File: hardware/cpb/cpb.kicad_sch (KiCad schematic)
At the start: 122 parts, among them J1 Conn_02x20_Odd_Even, J10 SW1, J11 SW2, J12 SW3, J13 PISW1, J14 μSW1, J15 μSW2, J16 μSW3, J17 μSW4, J2 I2CExt, J3 DAC1BUF, J4 DAC2BUF, J6 Conn_02x20_Odd_Even, J7 ADC6/7, J8 ADC2/3, J9 4FBRG, J99 RBFJUMP, Q1 PMBT2222A, Q2 IRF9393, Q3 MBT2222ADW1T1, Q4 PMBT2222A, U1 TS912, U2 ADR420ARMZ, U3 KF33BDT, U4 STM32L072R_B-Z_Tx, U5 AP63205WU, U6 SC16IS750xBS, Y1 14.7456MHz

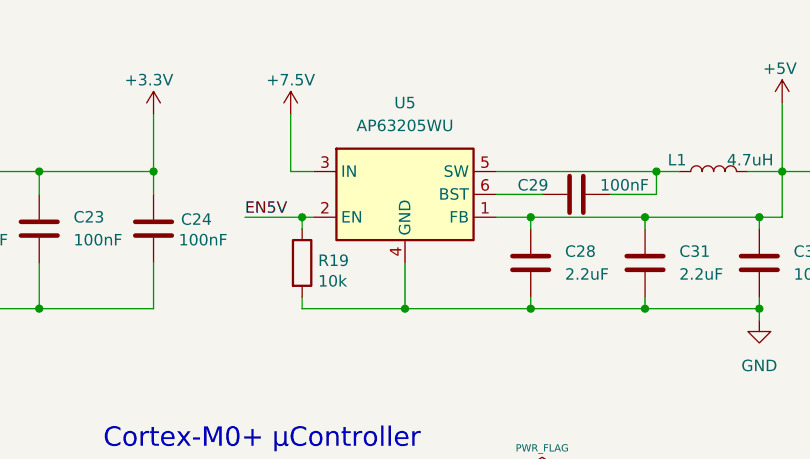
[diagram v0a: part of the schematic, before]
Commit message: cpb: many, many fixes
- Move components to bottom to match design intent
- Adjust AP62305 to hopefully have correct pinout
- Replace manual RBF jumper with solder jumper: just not enough room
- High level adjustment to placement to ease layout.
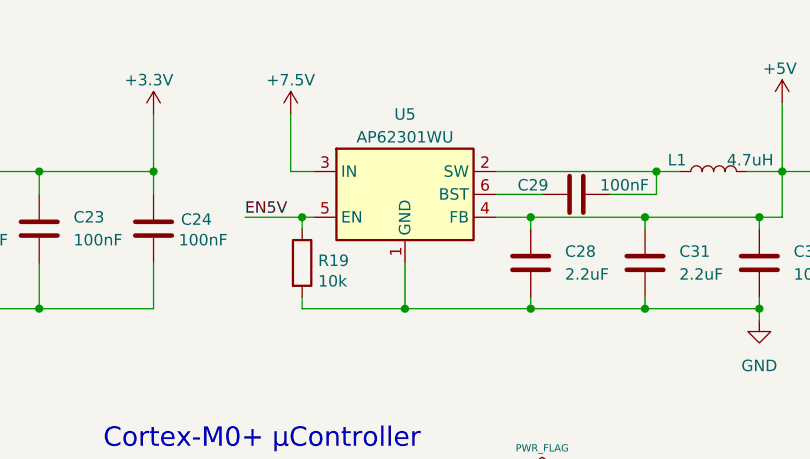
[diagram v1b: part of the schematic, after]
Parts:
- removed U5: AP63205WU, Package_TO_SOT_SMD:TSOT-23-6, symbol Regulator_Switching:AP63205WU
- added U5: AP62301WU, Package_TO_SOT_SMD:TSOT-23-6, symbol Regulator_Switching:AP62301WU
- J6: footprint Connector_PinHeader_2.54mm:PinHeader_2x20_P2.54mm_Vertical -> SSE_Footprints:RPI02W
- J99: footprint Connector_PinHeader_2.54mm:PinHeader_1x02_P2.54mm_Horizontal -> Jumper:SolderJumper-2_P1.3mm_Open_TrianglePad1.0x1.5mm
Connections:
- net +5V: now also U5.4 (FB)
- net +7.5V: now also U5.3 (IN)
- net EN5V: now also U5.5 (EN)
- net GND: now also U5.1 (GND)
- net at C29.2, L1.1: now also U5.2 (SW)
- net at C29.1: now also U5.6 (BST)
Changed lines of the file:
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@@
 	)
 	(symbol
+		(lib_id "Regulator_Switching:AP62301WU")
+		(at 205.74 31.75 0)
+		(unit 1)
+		(exclude_from_sim no)
+		(in_bom yes)
+		(on_board yes)
+		(dnp no)
+		(fields_autoplaced yes)
+		(property "Reference" "U5"
+			(at 205.74 22.86 0)
+			(effects
+				(font
+					(size 1.27 1.27)
+				)
+			)
+		)
+		(property "Value" "AP62301WU"
+			(at 205.74 25.4 0)
+			(effects
+				(font
+					(size 1.27 1.27)
+				)
+			)
+		)
+		(property "Footprint" "Package_TO_SOT_SMD:TSOT-23-6"
+			(at 205.74 54.61 0)
+			(effects
+				(font
+					(size 1.27 1.27)
+				)
+				(hide yes)
+			)
+		)
+		(property "Datasheet" "https://www.diodes.com/assets/Datasheets/AP62300_AP62301_AP62300T.pdf"
+			(at 205.74 31.75 0)
+			(effects
+				(font
+					(size 1.27 1.27)
+				)
+				(hide yes)
+			)
+		)
+		(property "Description" "3A, 750kHz Buck DC/DC Converter, 4.2V-18V input voltage, 0.8V-7V adjustable output voltage, TSOT-23-6"
+			(at 205.74 31.75 0)
+			(effects
+				(font
+					(size 1.27 1.27)
+				)
+				(hide yes)
+			)
+		)
+		(pin "6"
+		)
+		(pin "3"
+		)
+		(pin "5"
+		)
+		(pin "4"
+		)
+		(pin "1"
+		)
+		(pin "2"
+		)
+		(instances
+			(project "cpb"
+				(path "/9a10a1ee-db5a-47ad-90f3-81b92d74d449"
+					(reference "U5")
+					(unit 1)
+				)
+			)
+		)
+	)
+	(symbol
 		(lib_id "power:GND")
 		(at 193.04 224.79 0)
@@
 	)
 	(symbol
-		(lib_id "Regulator_Switching:AP63205WU")
-		(at 205.74 31.75 0)
-		(unit 1)
-		(exclude_from_sim no)
-		(in_bom yes)
-		(on_board yes)
-		(dnp no)
-		(fields_autoplaced yes)
-		(property "Reference" "U5"
-			(at 205.74 21.59 0)
-			(effects
-				(font
-					(size 1.27 1.27)
-				)
-			)
-		)
-		(property "Value" "AP63205WU"
-			(at 205.74 24.13 0)
-			(effects
-				(font
-					(size 1.27 1.27)
-				)
-			)
-		)
-		(property "Footprint" "Package_TO_SOT_SMD:TSOT-23-6"
-			(at 205.74 54.61 0)
-			(effects
-				(font
-					(size 1.27 1.27)
-				)
-				(hide yes)
-			)
-		)
-		(property "Datasheet" "https://www.diodes.com/assets/Datasheets/AP63200-AP63201-AP63203-AP63205.pdf"
-			(at 205.74 31.75 0)
-			(effects
-				(font
-					(size 1.27 1.27)
-				)
-				(hide yes)
-			)
-		)
-		(property "Description" "2A, 1.1MHz Buck DC/DC Converter, fixed 5.0V output voltage, TSOT-23-6"
-			(at 205.74 31.75 0)
-			(effects
-				(font
-					(size 1.27 1.27)
-				)
-				(hide yes)
-			)
-		)
-		(property "LCSC" "C2071056"
-			(at 205.74 31.75 0)
-			(effects
-				(font
-					(size 1.27 1.27)
-				)
-				(hide yes)
-			)
-		)
-		(pin "1"
-		)
-		(pin "2"
-		)
-		(pin "6"
-		)
-		(pin "5"
-		)
-		(pin "3"
-		)
-		(pin "4"
-		)
-		(instances
-			(project "cpb"
-				(path "/9a10a1ee-db5a-47ad-90f3-81b92d74d449"
-					(reference "U5")
-					(unit 1)
-				)
-			)
-		)
-	)
-	(symbol
 		(lib_id "power:GND")
 		(at 403.86 138.43 0)
@@
 			)
 		)
-		(property "Footprint" "Connector_PinHeader_2.54mm:PinHeader_1x02_P2.54mm_Horizontal"
+		(property "Footprint" "Jumper:SolderJumper-2_P1.3mm_Open_TrianglePad1.0x1.5mm"
 			(at 134.62 125.73 0)
 			(effects
@@
 			)
 		)
-		(property "Footprint" "Connector_PinHeader_2.54mm:PinHeader_2x20_P2.54mm_Vertical"
+		(property "Footprint" "SSE_Footprints:RPI02W"
 			(at 269.24 228.6 0)
 			(effects

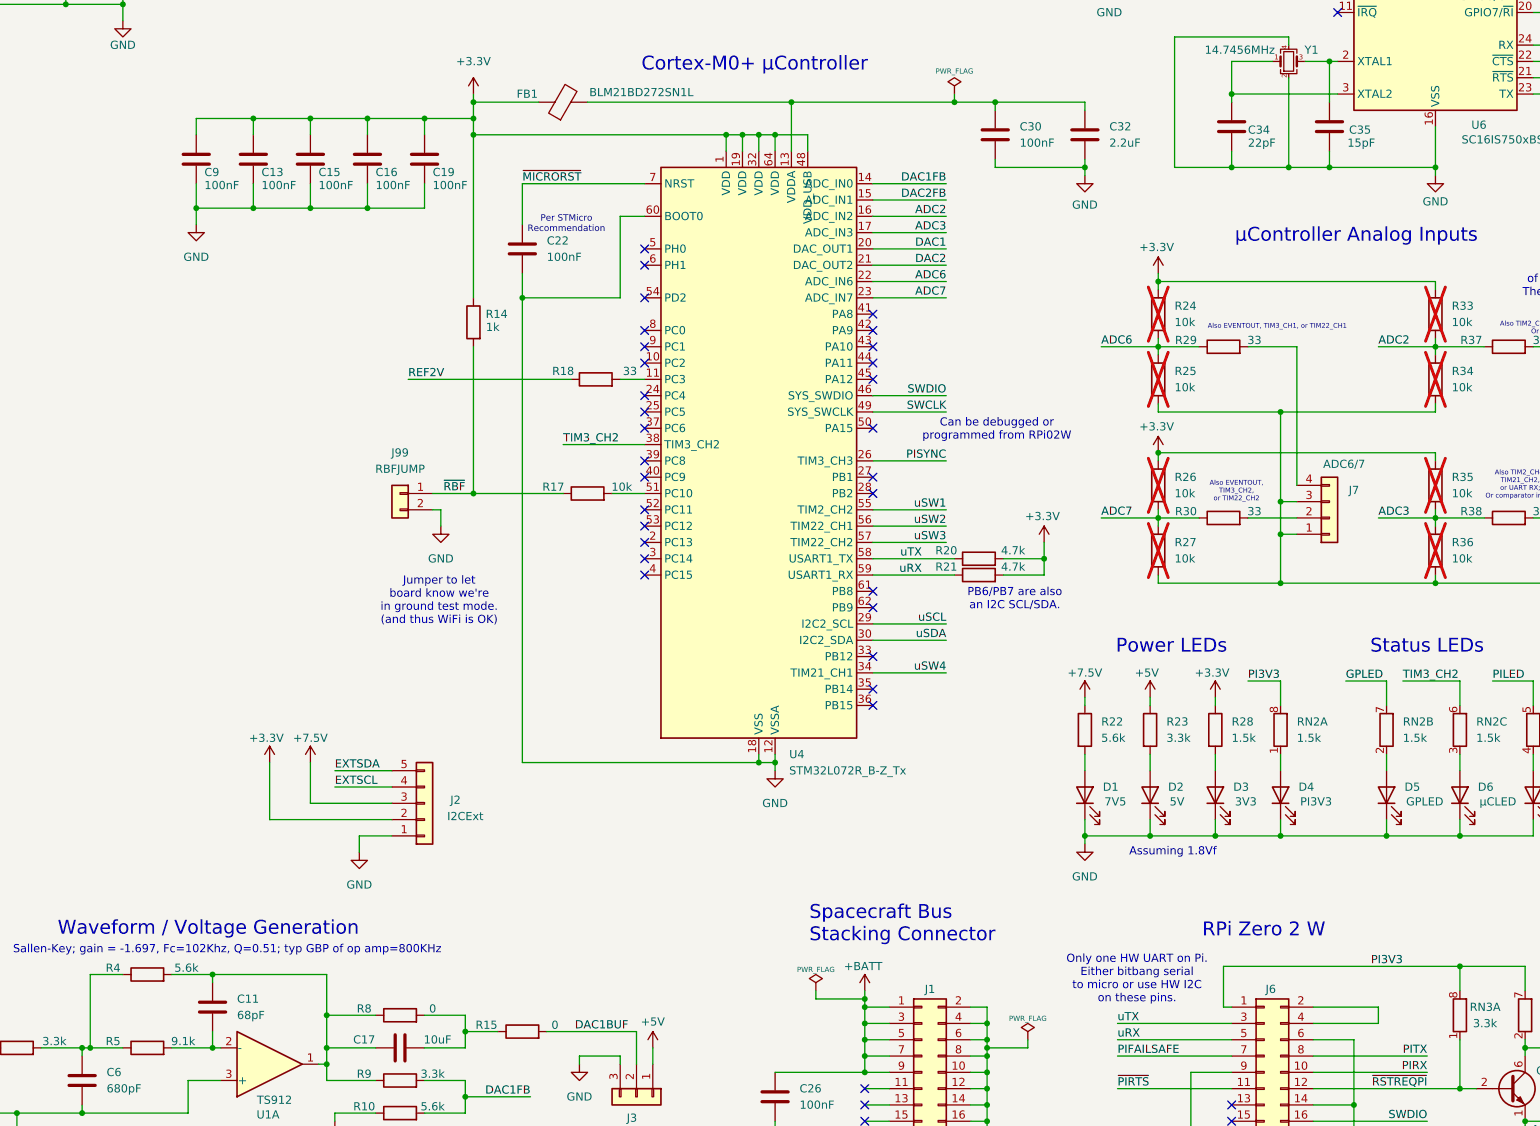
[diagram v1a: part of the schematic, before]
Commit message: cpb: complete placement
- add a capacitor to ensure we can bypass all 3V3 components well
- align components
- add copper pour regions
- a lot of effort on text, and legends for connectors

Plus probably much more...
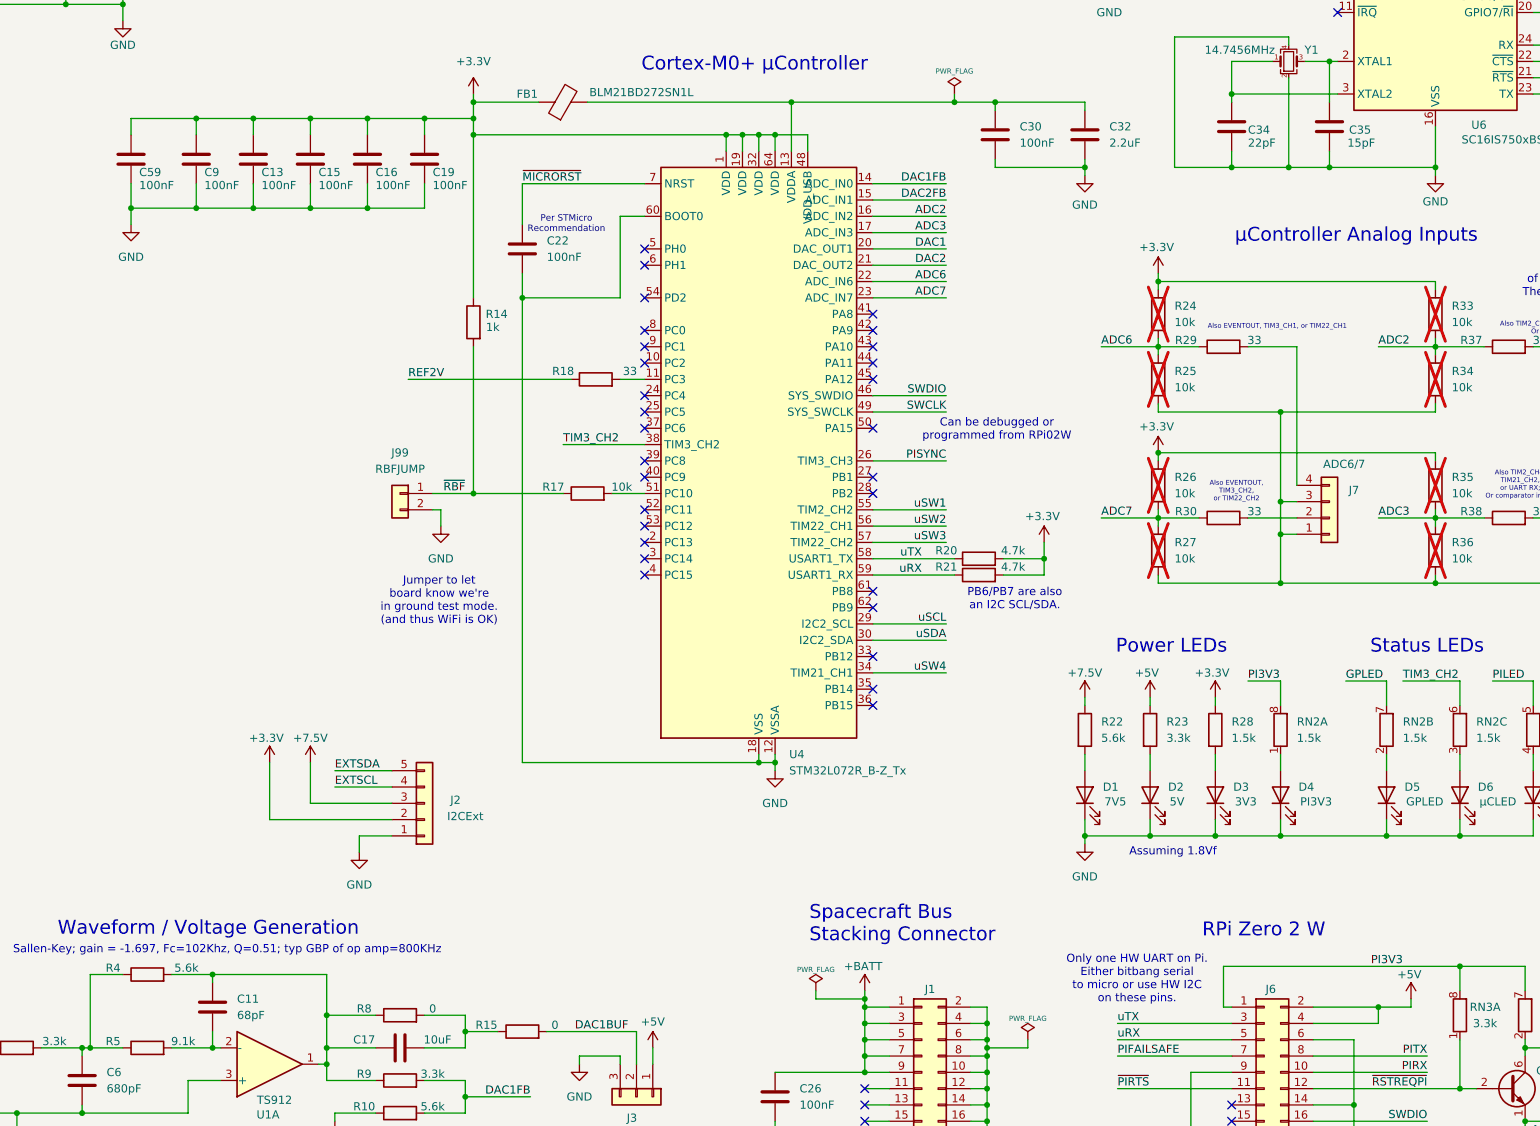
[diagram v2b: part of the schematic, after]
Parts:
- added C59: 100nF, Capacitor_SMD:C_0603_1608Metric, symbol Device:C
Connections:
- net +3.3V: now also C59.1
- net +5V: now also J6.2 (Pin_2), J6.4 (Pin_4)
- net GND: now also C59.2
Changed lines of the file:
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@@
 	)
 	(junction
+		(at 102.87 67.31)
+		(diameter 0)
+		(color 0 0 0 0)
+	)
+	(junction
 		(at 262.89 27.94)
 		(diameter 0)
@@
 	)
 	(junction
+		(at 92.71 81.28)
+		(diameter 0)
+		(color 0 0 0 0)
+	)
+	(junction
 		(at 299.72 218.44)
 		(diameter 0)
@@
 	)
 	(junction
+		(at 287.02 205.74)
+		(diameter 0)
+		(color 0 0 0 0)
+	)
+	(junction
 		(at 193.04 69.85)
 		(diameter 0)
@@
 	(wire
 		(pts
-			(xy 102.87 81.28) (xy 102.87 83.82)
+			(xy 92.71 81.28) (xy 92.71 83.82)
 		)
 		(stroke
@@
 	(wire
 		(pts
+			(xy 92.71 77.47) (xy 92.71 81.28)
+		)
+		(stroke
+			(width 0)
+			(type default)
+		)
+	)
+	(wire
+		(pts
 			(xy 146.05 125.73) (xy 160.02 125.73)
 		)
@@
 	(wire
 		(pts
+			(xy 92.71 69.85) (xy 92.71 67.31)
+		)
+		(stroke
+			(width 0)
+			(type default)
+		)
+	)
+	(wire
+		(pts
 			(xy 226.06 223.52) (xy 226.06 226.06)
 		)
@@
 	(wire
 		(pts
+			(xy 292.1 204.47) (xy 292.1 205.74)
+		)
+		(stroke
+			(width 0)
+			(type default)
+		)
+	)
+	(wire
+		(pts
 			(xy 91.44 25.4) (xy 91.44 24.13)
 		)
@@
 	(wire
 		(pts
+			(xy 292.1 205.74) (xy 287.02 205.74)
+		)
+		(stroke
+			(width 0)
+			(type default)
+		)
+	)
+	(wire
+		(pts
 			(xy 52.07 21.59) (xy 57.15 21.59)
 		)
@@
 	(wire
 		(pts
+			(xy 92.71 67.31) (xy 102.87 67.31)
+		)
+		(stroke
+			(width 0)
+			(type default)
+		)
+	)
+	(wire
+		(pts
 			(xy 314.96 139.7) (xy 295.91 139.7)
 		)
@@
 	(wire
 		(pts
+			(xy 92.71 81.28) (xy 102.87 81.28)
+		)
+		(stroke
+			(width 0)
+			(type default)
+		)
+	)
+	(wire
+		(pts
 			(xy 226.06 226.06) (xy 226.06 228.6)
 		)
@@
 	)
 	(symbol
+		(lib_id "power:+5V")
+		(at 292.1 204.47 0)
+		(unit 1)
+		(exclude_from_sim no)
+		(in_bom yes)
+		(on_board yes)
+		(dnp no)
+		(property "Reference" "#PWR076"
+			(at 292.1 208.28 0)
+			(effects
+				(font
+					(size 1.27 1.27)
+				)
+				(hide yes)
+			)
+		)
+		(property "Value" "+5V"
+			(at 291.846 200.66 0)
+			(effects
+				(font
+					(size 1.27 1.27)
+				)
+			)
+		)
+		(property "Footprint" ""
+			(at 292.1 204.47 0)
+			(effects
+				(font
+					(size 1.27 1.27)
+				)
+				(hide yes)
+			)
+		)
+		(property "Datasheet" ""
+			(at 292.1 204.47 0)
+			(effects
+				(font
+					(size 1.27 1.27)
+				)
+				(hide yes)
+			)
+		)
+		(property "Description" "Power symbol creates a global label with name \"+5V\""
+			(at 292.1 204.47 0)
+			(effects
+				(font
+					(size 1.27 1.27)
+				)
+				(hide yes)
+			)
+		)
+		(pin "1"
+		)
+		(instances
+			(project "cpb"
+				(path "/9a10a1ee-db5a-47ad-90f3-81b92d74d449"
+					(reference "#PWR076")
+					(unit 1)
+				)
+			)
+		)
+	)
+	(symbol
 		(lib_id "Device:C")
 		(at 232.41 39.37 0)
@@
 	(symbol
 		(lib_id "power:GND")
-		(at 102.87 83.82 0)
+		(at 92.71 83.82 0)
 		(unit 1)
 		(exclude_from_sim no)
@@
 		(dnp no)
 		(property "Reference" "#PWR013"
-			(at 102.87 90.17 0)
+			(at 92.71 90.17 0)
 			(effects
 				(font
@@
 		)
 		(property "Value" "GND"
-			(at 102.87 88.9 0)
+			(at 92.71 88.9 0)
 			(effects
 				(font
@@
 		)
 		(property "Footprint" ""
-			(at 102.87 83.82 0)
+			(at 92.71 83.82 0)
 			(effects
 				(font
@@
 		)
 		(property "Datasheet" ""
-			(at 102.87 83.82 0)
+			(at 92.71 83.82 0)
 			(effects
 				(font
@@
 		)
 		(property "Description" "Power symbol creates a global label with name \"GND\" , ground"
-			(at 102.87 83.82 0)
+			(at 92.71 83.82 0)
 			(effects
 				(font
@@
 					(unit 1)
 				)
+			)
+		)
+	)
+	(symbol
+		(lib_id "Device:C")
+		(at 92.71 73.66 0)
+		(unit 1)
+		(exclude_from_sim no)
+		(in_bom yes)
+		(on_board yes)
+		(dnp no)
+		(property "Reference" "C59"
+			(at 93.98 75.692 0)
+			(effects
+				(font
+					(size 1.27 1.27)
+				)
+				(justify left)
+			)
+		)
+		(property "Value" "100nF"
+			(at 93.98 77.724 0)
+			(effects
+				(font
+					(size 1.27 1.27)
+				)
+				(justify left)
+			)
+		)
+		(property "Footprint" "Capacitor_SMD:C_0603_1608Metric"
+			(at 93.6752 77.47 0)
+			(effects
+				(font
+					(size 1.27 1.27)
+				)
+				(hide yes)
+			)
+		)
+		(property "Datasheet" "~"
+			(at 92.71 73.66 0)
+			(effects
+				(font
+					(size 1.27 1.27)
+				)
+				(hide yes)
+			)
+		)
+		(property "Description" "Unpolarized capacitor"
+			(at 92.71 73.66 0)
+			(effects
+				(font
+					(size 1.27 1.27)
+				)
+				(hide yes)
+			)
+		)
+		(pin "1"
+		)
+		(pin "2"
+		)
+		(instances
+			(project "cpb"
+				(path "/9a10a1ee-db5a-47ad-90f3-81b92d74d449"
+					(reference "C59")
+					(unit 1)
+				)
